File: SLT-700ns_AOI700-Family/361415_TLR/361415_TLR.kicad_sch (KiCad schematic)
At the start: 9 parts, among them T1 CB, T2 CC, T3 CB, U1 12-Pin_SLx_Can

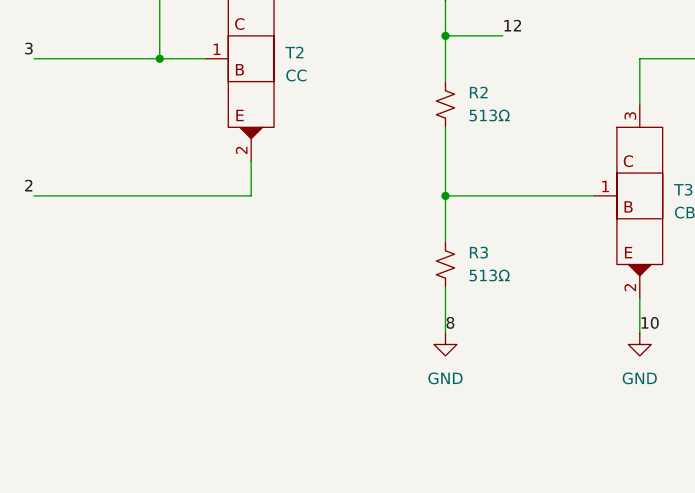
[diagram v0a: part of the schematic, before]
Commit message: Add can P/N to schematics for SLT-700
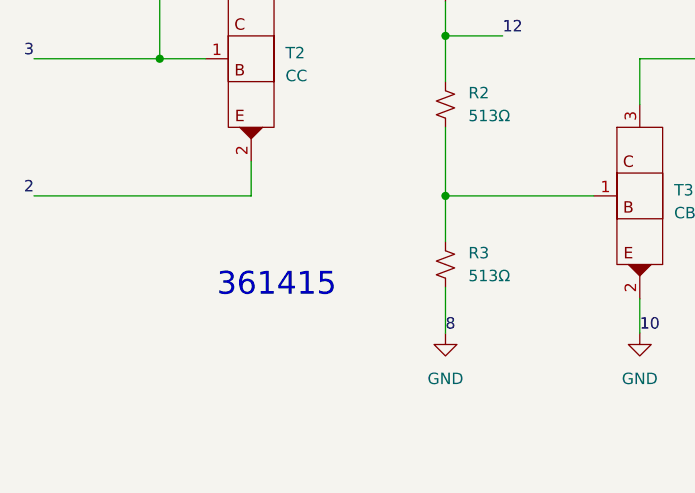
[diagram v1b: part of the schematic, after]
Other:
- note added: "361415"
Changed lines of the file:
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@@
     (effects (font (size 1.27 1.27)) (justify left bottom))
+  )
+  (text "361415" (at 106.68 128.27 0)
+    (effects (font (size 2.54 2.54)) (justify left bottom))
   )
   (label "8" (at 132.08 132.08 0)
